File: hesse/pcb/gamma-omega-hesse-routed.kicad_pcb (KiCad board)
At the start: 2 copper layers, 232.8 x 111.4 mm, 45 parts

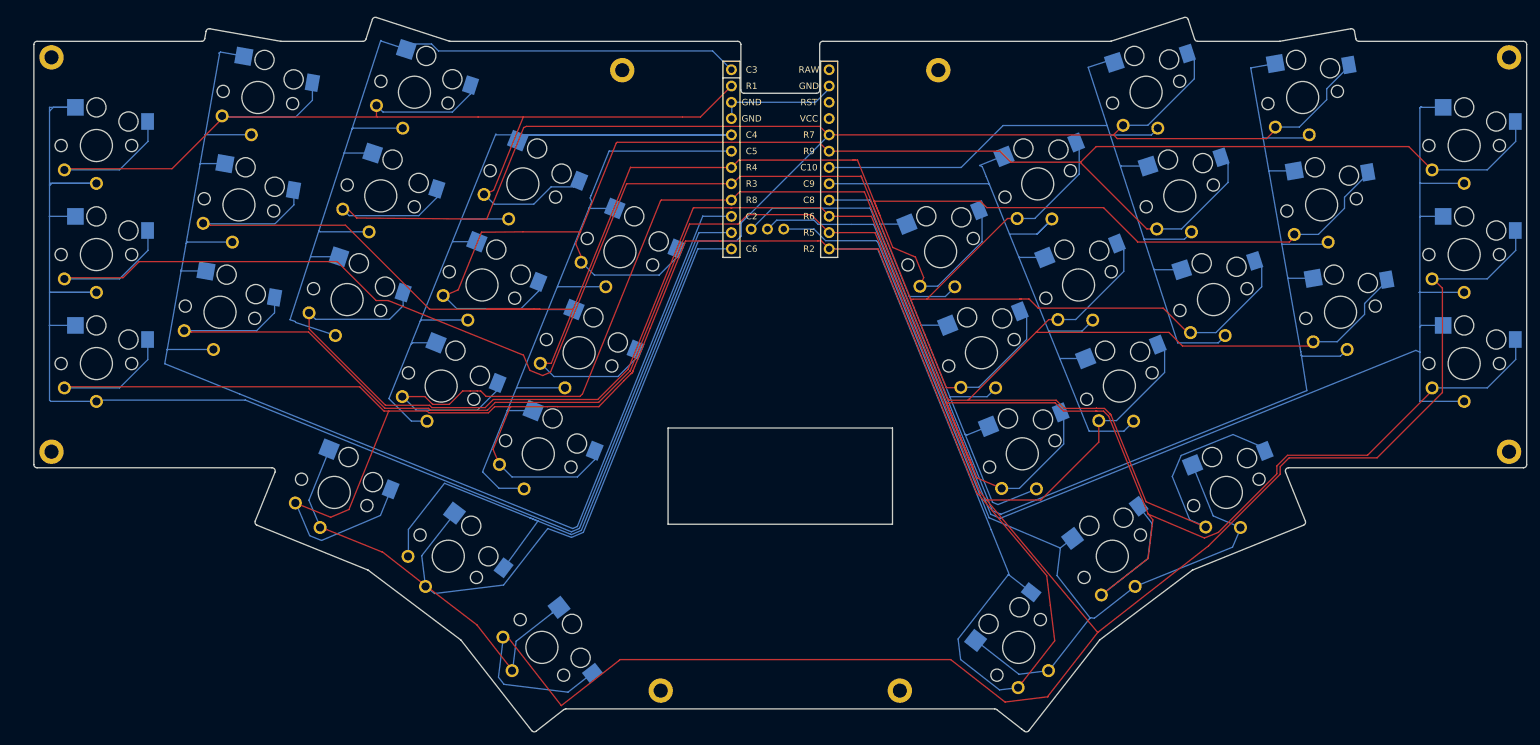
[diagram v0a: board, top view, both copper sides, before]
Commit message: Routing including JST power socket (0.4 traces, more than enough?)
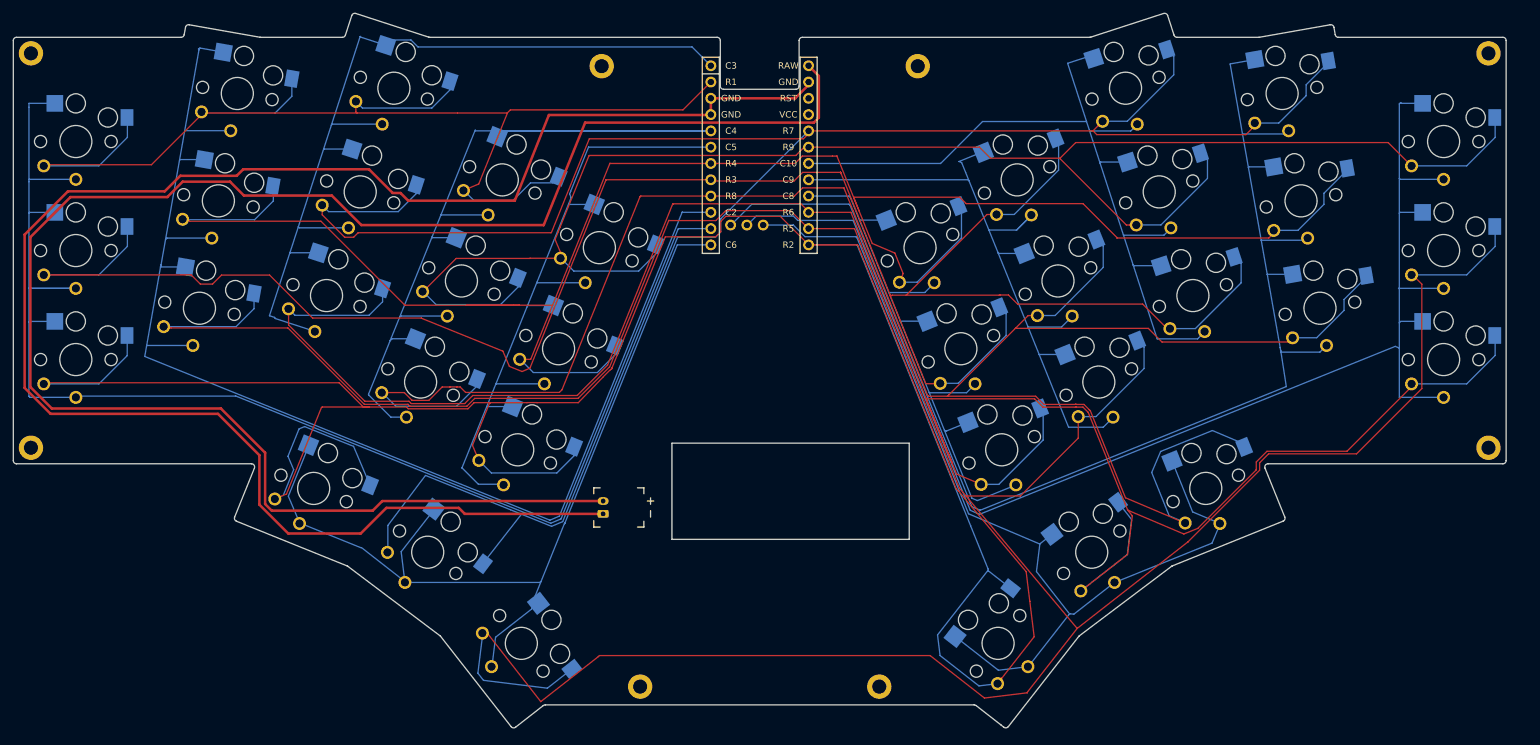
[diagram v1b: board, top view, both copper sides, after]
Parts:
- added JST1: , ceoloide:battery_connector_jst_ph_2, F.Cu at (125.5, 124.8)
- moved S29 3.27 mm to (196.4, 89.5)
- moved S23 3.27 mm to (234.3, 77.0)
- moved H2 3.27 mm to (263.5, 54.0)
- moved S35 3.27 mm to (201.7, 131.8)
- moved S33 3.27 mm to (174.9, 84.3)
- moved S26 3.27 mm to (212.2, 75.6)
- moved S15 3.27 mm to (124.9, 84.3)
- moved S3 3.27 mm to (43.2, 67.7)
- moved S20 3.27 mm to (256.5, 84.7)
- moved S11 3.27 mm to (103.4, 89.5)
- moved S25 3.27 mm to (217.4, 91.8)
- moved S9 3.27 mm to (92.8, 59.4)
- moved S14 3.27 mm to (118.5, 100.0)
- moved H1 3.27 mm to (36.2, 54.0)
- moved MCU1 3.27 mm to (149.9, 68.6)
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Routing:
- net RAW: track 0.00 -> 275.2 mm
- net GND: track 18.7 -> 289.7 mm
- net C6: track 159.2 -> 145.0 mm
- net C1: track 233.5 -> 220.6 mm
- net R2: track 408.6 -> 417.0 mm
- net R9: track 265.7 -> 258.9 mm
- net R7: track 336.1 -> 337.8 mm
- net C2: track 209.5 -> 208.2 mm
- net R4: track 306.2 -> 305.1 mm
- net R1: track 194.8 -> 195.3 mm
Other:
- outline, holes or cut-outs redrawn

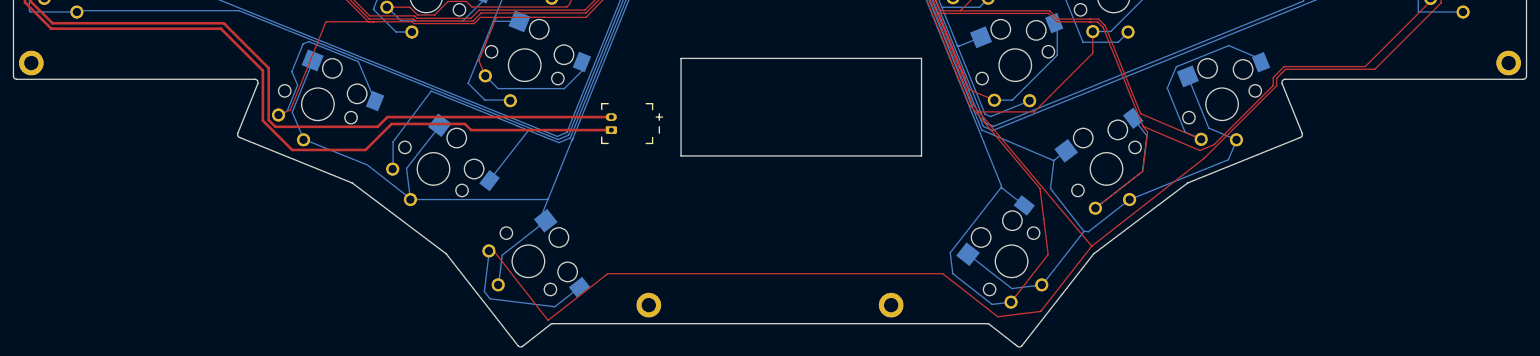
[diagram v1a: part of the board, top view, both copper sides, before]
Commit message: Copy-and-paste, may have moved screw holes?
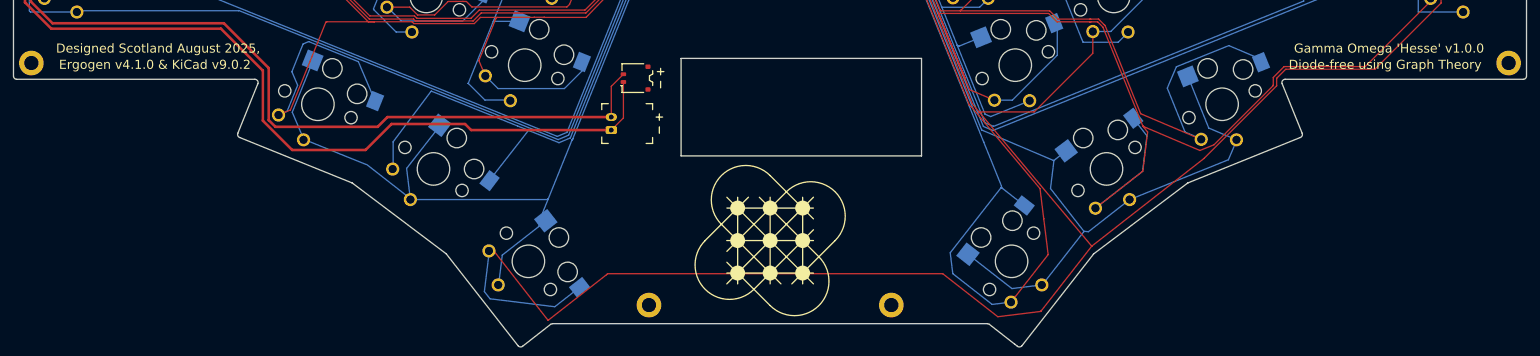
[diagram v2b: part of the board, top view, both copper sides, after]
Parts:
- added CONN1: , ceoloide:battery_connector_molex_pico_ezmate_1x02, F.Cu at (129.2, 117.8)
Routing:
- net GND: track 289.7 -> 297.8 mm
- net RAW: track 275.2 -> 282.5 mm
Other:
- board text added: "(GPIO pins),"
- board text added: "(keys)."
- board text added: "36 edges"
- board text added: "9+12=21 nodes,"
- board text added: "Configuration"
- board text added: "Designed Scotland August 2025,"
- board text added: "Diode-free using Graph Theory"
- board text added: "Ergogen v4.1.0 & KiCad v9.0.2"
- board text added: "Gamma Omega 'Hesse' v1.0.0"
- board text added: "Hesse"
- board text added: "Incidence Graph,"
- board text added: "Keyboard uses its"
- board text added: "of 9 points,"
- board text added: "on 12 lines."

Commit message: Move routed PCB to almost where Ergogen places it
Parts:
- moved H7 6.96 mm to (138.0, 151.0)
- moved H8 6.96 mm to (175.3, 151.0)
- moved S33 6.96 mm to (181.6, 82.6)
- moved S35 6.96 mm to (208.4, 130.1)
- moved CONN1 6.96 mm to (135.9, 116.1)
- moved H2 6.96 mm to (270.3, 52.3)
- moved H4 6.96 mm to (270.3, 113.8)
- moved H6 6.96 mm to (181.3, 54.3)
- moved S19 6.96 mm to (263.3, 100.0)
- moved S20 6.96 mm to (263.3, 83.0)
- moved S21 6.96 mm to (263.3, 66.0)
- moved S23 6.96 mm to (241.0, 75.3)
- moved S24 6.96 mm to (238.1, 58.5)
- moved S30 6.96 mm to (196.8, 72.0)
- moved S31 6.96 mm to (194.4, 114.1)
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
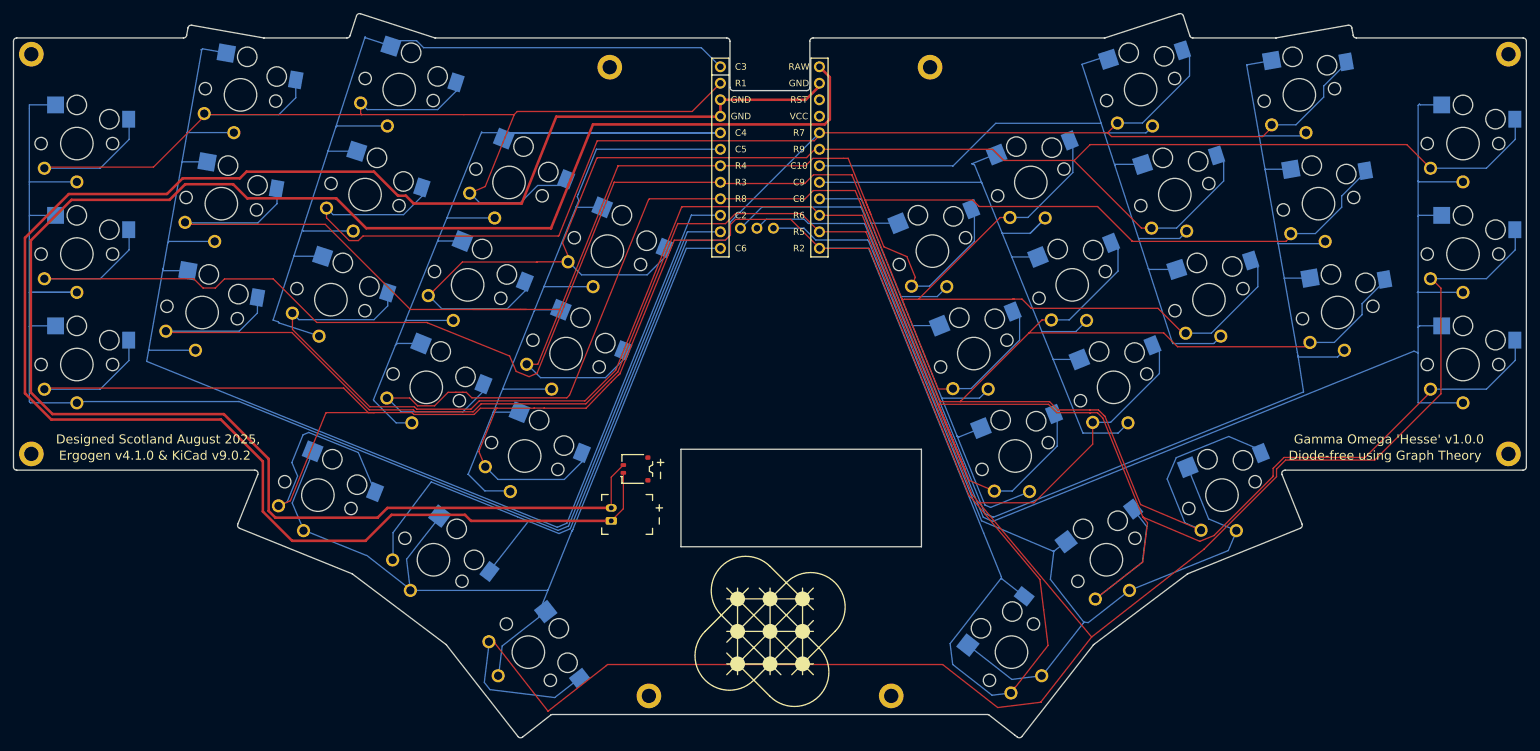
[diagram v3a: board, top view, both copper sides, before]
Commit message: Apply manual traces to fresh Ergogen output (moved battery etc)
The recent Ergogen changes include a larger battery cutout,
moving the battery connectors, and auto-tracing for each
switch and column. Used Ergogen Helper copy-traces and then
addressed the slight wiring duplication & tolerances.
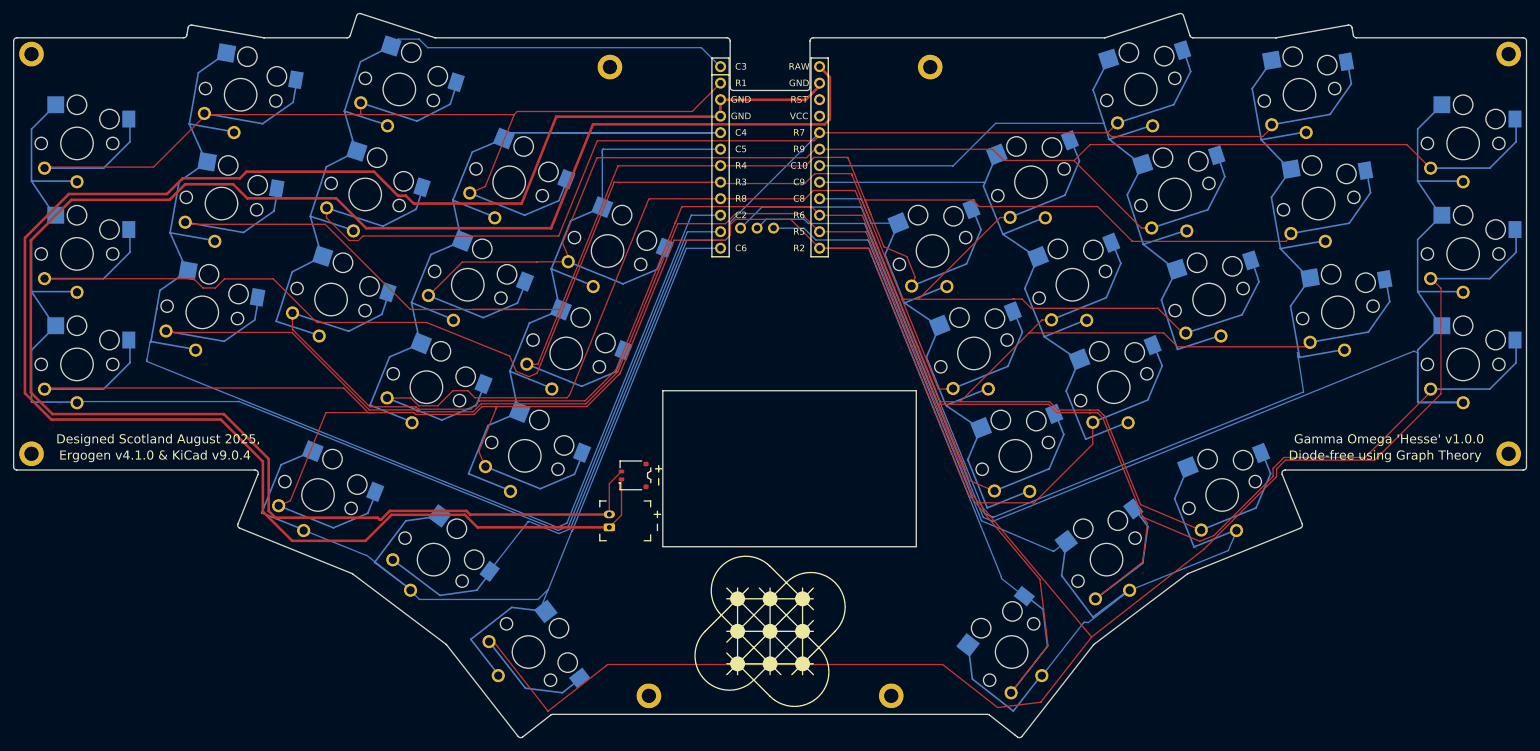
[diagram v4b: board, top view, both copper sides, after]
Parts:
- moved JST1 1.03 mm to (131.9, 124.1)
- moved CONN1 1.03 mm to (135.7, 117.1)
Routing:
- net C4: track 201.3 -> 161.9 mm
- net C6: track 145.0 -> 167.0 mm
- net C7: track 154.0 -> 174.8 mm
- net R2: track 417.0 -> 399.3 mm
- net C1: track 220.6 -> 205.6 mm
- net C9: track 108.6 -> 97.9 mm
- net C3: track 134.2 -> 124.0 mm
- net R7: track 337.8 -> 328.3 mm
- net C10: track 128.2 -> 118.9 mm
- net C12: track 216.5 -> 225.3 mm
- net C5: track 107.5 -> 100.3 mm
- net C2: track 208.2 -> 201.0 mm
- net R8: track 326.5 -> 320.3 mm
- net C11: track 208.1 -> 202.5 mm
- net C8: track 92.7 -> 87.0 mm
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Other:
- outline, holes or cut-outs redrawn
- board text added: "Ergogen v4.1.0 & KiCad v9.0.4"
- board text removed: "Ergogen v4.1.0 & KiCad v9.0.2"

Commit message: polish
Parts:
- moved S9 0.45 mm to (99.4, 58.1)
- moved JST1 0.45 mm to (131.7, 124.5)
- moved H5 0.45 mm to (131.8, 54.6)
- moved S22 0.45 mm to (243.8, 92.4)
- moved S3 0.45 mm to (49.8, 66.4)
- moved S15 0.45 mm to (131.4, 82.9)
- moved H2 0.45 mm to (270.1, 52.6)
- moved H1 0.45 mm to (42.8, 52.6)
- moved H8 0.45 mm to (175.1, 151.4)
- moved S23 0.45 mm to (240.9, 75.6)
- moved S24 0.45 mm to (237.9, 58.9)
- moved H3 0.45 mm to (42.8, 114.1)
- moved S12 0.45 mm to (116.3, 72.4)
- moved S10 0.45 mm to (103.6, 103.9)
- moved S28 0.45 mm to (209.3, 103.9)
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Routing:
- net C6: track 167.0 -> 153.8 mm
- net C10: track 118.9 -> 126.9 mm
- net C2: track 201.0 -> 208.8 mm
- net C12: track 225.3 -> 217.6 mm
- net C9: track 97.9 -> 102.8 mm
- net C7: track 174.8 -> 171.2 mm
- net C11: track 202.5 -> 201.5 mm
- net R6: track 363.4 -> 364.3 mm
- net GND: track 298.0 -> 298.5 mm
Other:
- outline, holes or cut-outs redrawn

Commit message: clean
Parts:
- moved CONN1 0.43 mm to (135.2, 117.2)
- moved S24 0.37 mm to (237.6, 58.7)
- moved S4 0.37 mm to (68.8, 92.2)
- moved S6 0.37 mm to (74.7, 58.7)
- moved S12 0.37 mm to (116.0, 72.2)
- moved S31 0.37 mm to (193.9, 114.2)
- moved S10 0.37 mm to (103.3, 103.7)
- moved H6 0.37 mm to (180.8, 54.4)
- moved S8 0.37 mm to (93.9, 74.0)
- moved S9 0.37 mm to (99.1, 57.9)
- moved S15 0.37 mm to (131.2, 82.7)
- moved S5 0.37 mm to (71.7, 75.4)
- moved S23 0.37 mm to (240.6, 75.4)
- moved JST1 0.37 mm to (131.4, 124.2)
- moved S21 0.37 mm to (262.8, 66.2)
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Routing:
- net R5: track 495.9 -> 569.3 mm
- net R7: track 328.3 -> 401.3 mm
- net R1: track 198.1 -> 271.0 mm
- net R4: track 308.9 -> 381.7 mm
- net R9: track 259.0 -> 331.8 mm
- net R3: track 327.5 -> 400.2 mm
- net C1: track 205.6 -> 278.1 mm
- net C4: track 161.9 -> 234.3 mm
- net C3: track 124.0 -> 196.4 mm
- net C9: track 102.8 -> 175.2 mm
- net C5: track 100.3 -> 172.7 mm
- net C8: track 87.0 -> 159.4 mm
- net C12: track 217.6 -> 289.9 mm
- net C11: track 201.5 -> 273.8 mm
- net C10: track 126.9 -> 199.3 mm
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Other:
- outline, holes or cut-outs redrawn

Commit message: shift
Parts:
- moved S14 0.26 mm to (125.0, 98.4)
- moved S5 0.26 mm to (72.0, 75.3)
- moved S2 0.26 mm to (49.8, 83.1)
- moved S12 0.26 mm to (116.3, 72.1)
- moved JST1 0.26 mm to (131.7, 124.2)
- moved S7 0.26 mm to (88.8, 90.1)
- moved S35 0.26 mm to (208.2, 130.1)
- moved S25 0.26 mm to (223.9, 90.1)
- moved H6 0.26 mm to (181.0, 54.3)
- moved H3 0.26 mm to (42.8, 113.8)
- moved S15 0.26 mm to (131.4, 82.6)
- moved S1 0.26 mm to (49.8, 100.1)
- moved H1 0.26 mm to (42.8, 52.3)
- moved S11 0.26 mm to (109.9, 87.8)
- moved S33 0.26 mm to (181.4, 82.6)
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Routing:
- net R7: track 401.3 -> 474.2 mm
- net R9: track 331.8 -> 404.8 mm
- net R3: track 400.2 -> 473.1 mm
- net R1: track 271.0 -> 343.9 mm
- net R8: track 390.5 -> 463.4 mm
- net R6: track 435.9 -> 508.8 mm
- net R2: track 471.0 -> 543.9 mm
- net R5: track 569.3 -> 642.2 mm
- net R4: track 381.7 -> 454.6 mm
- net C12: track 289.9 -> 362.3 mm
- net C9: track 175.2 -> 247.6 mm
- net C5: track 172.7 -> 245.0 mm
- net C1: track 278.1 -> 350.4 mm
- net C8: track 159.4 -> 231.8 mm
- net C2: track 281.1 -> 353.4 mm
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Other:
- outline, holes or cut-outs redrawn

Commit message: clean
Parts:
- moved H1 0.77 mm to (42.0, 52.5)
- moved S15 0.77 mm to (130.6, 82.8)
- moved H6 0.77 mm to (180.3, 54.5)
- moved H5 0.77 mm to (131.0, 54.5)
- moved S14 0.77 mm to (124.3, 98.5)
- moved S1 0.77 mm to (49.0, 100.2)
- moved H2 0.77 mm to (269.3, 52.5)
- moved S7 0.77 mm to (88.1, 90.2)
- moved S6 0.77 mm to (74.2, 58.7)
- moved S12 0.77 mm to (115.5, 72.2)
- moved S21 0.77 mm to (262.3, 66.2)
- moved S5 0.77 mm to (71.2, 75.5)
- moved CONN1 0.77 mm to (134.6, 117.3)
- moved H4 0.77 mm to (269.3, 114.0)
- moved S27 0.77 mm to (212.7, 57.9)
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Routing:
- net R2: track 543.9 -> 531.7 mm
- net R5: track 642.2 -> 641.5 mm
- net R3: track 473.1 -> 472.4 mm
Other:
- outline, holes or cut-outs redrawn
